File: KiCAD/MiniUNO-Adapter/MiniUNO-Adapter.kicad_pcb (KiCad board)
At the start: 2 copper layers, 3 parts, among them J1 Conn_01x11, J2 Conn_01x11, J3 Conn_01x07

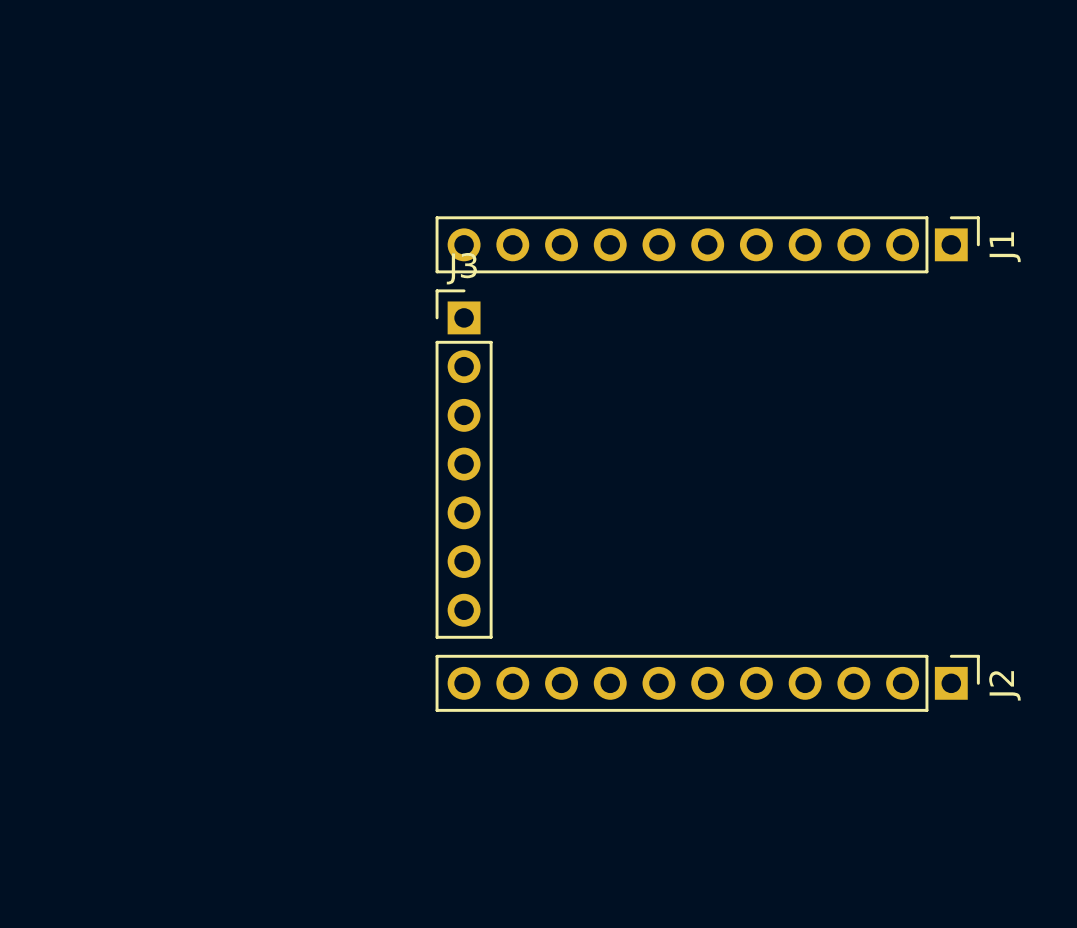
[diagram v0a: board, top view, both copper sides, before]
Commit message: Addec pulldown resistors to the VUSB and VIN MOSFETS. Made the adapter PCB
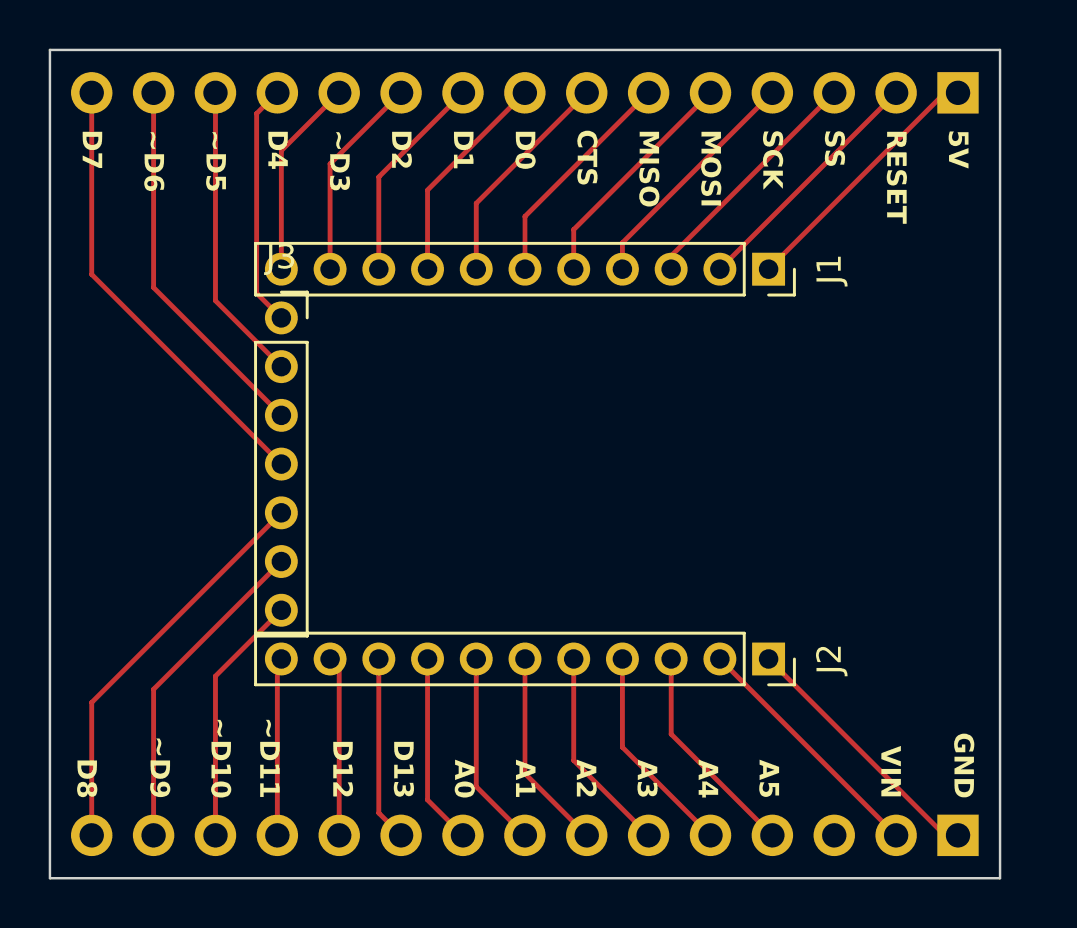
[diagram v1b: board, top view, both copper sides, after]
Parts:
- added J4: Conn_01x15, Connector_PinHeader_2.54mm:PinHeader_1x15_P2.54mm_Vertical, B.Cu at (17.8, -15.2)
- added J5: Conn_01x15, Connector_PinHeader_2.54mm:PinHeader_1x15_P2.54mm_Vertical, B.Cu at (17.8, 15.2)
- J1, J2: footprint Connector_PinHeader_2.00mm:PinHeader_1x11_P2.00mm_Vertical -> Connector_PinSocket_2.00mm:PinSocket_1x11_P2.00mm_Vertical
- J3: footprint Connector_PinHeader_2.00mm:PinHeader_1x07_P2.00mm_Vertical -> Connector_PinSocket_2.00mm:PinSocket_1x07_P2.00mm_Vertical
- moved J1 7.57 mm to (10.0, -8.00)
- moved J2 7.57 mm to (10.0, 8.00)
- moved J3 7.50 mm to (-10.0, -6.00)
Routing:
- net D7: track 0.00 -> 18.5 mm
- net D8: track 0.00 -> 16.5 mm
- net D6: track 0.00 -> 15.4 mm
- net D9: track 0.00 -> 13.4 mm
- net D5: track 0.00 -> 12.4 mm
- net GND: track 0.00 -> 10.8 mm
- net +5V: track 0.00 -> 10.8 mm
- net D10: track 0.00 -> 10.4 mm
- net VIN: track 0.00 -> 10.2 mm
- net RESET: track 0.00 -> 10.2 mm
- net SS: track 0.00 -> 10.0 mm
- net D4: track 0.00 -> 10.0 mm
- net SCK: track 0.00 -> 9.79 mm
- net MOSI: track 0.00 -> 9.57 mm
- net MISO: track 0.00 -> 9.34 mm
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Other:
- board outline added: 39 x 34 mm
- board text added: "5V"
- board text added: "A0"
- board text added: "A1"
- board text added: "A2"
- board text added: "A3"
- board text added: "A4"
- board text added: "A5"
- board text added: "CTS"
- board text added: "D0"
- board text added: "D1"
- board text added: "D12"
- board text added: "D13"
- board text added: "D2"
- board text added: "D4"
- board text added: "D7"
- board text added: "D8"
- board text added: "GND"
- board text added: "MISO"
- board text added: "MOSI"
- board text added: "RESET"
- board text added: "SCK"
- board text added: "SS"
- board text added: "VIN"
- board text added: "~D10"
- board text added: "~D11"
- board text added: "~D3"
- board text added: "~D5"
- board text added: "~D6"
- board text added: "~D9"
